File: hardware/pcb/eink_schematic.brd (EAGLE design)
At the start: 90.2 x 71.1 mm, 13 parts, among them J1 AA_BAT_PACKSMD, J2 5.5x2.1mm Barrel, Q1 FDN340P, U1 NUCLEUM, U2 LTC3531ES6-3PBF, U4 MAX6326UR29+

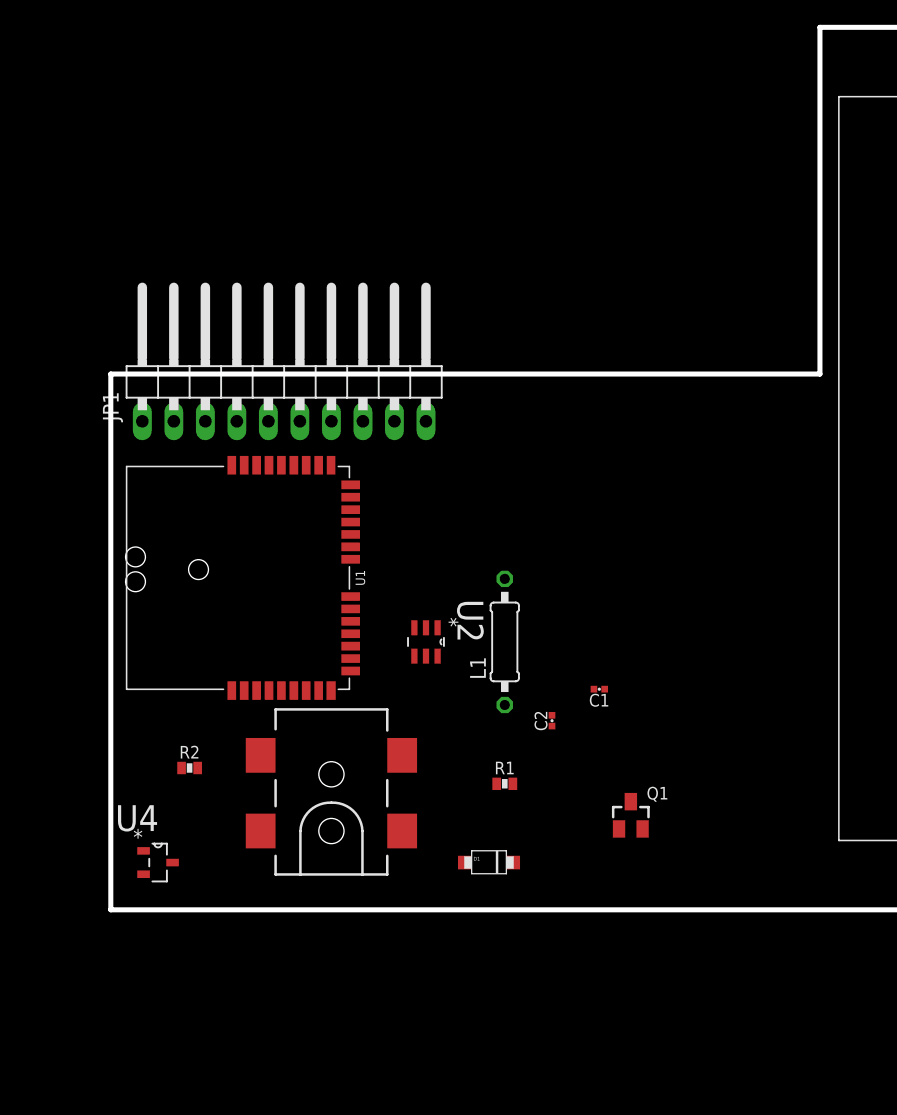
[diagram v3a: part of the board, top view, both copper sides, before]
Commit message: added digikey part numbers for everything
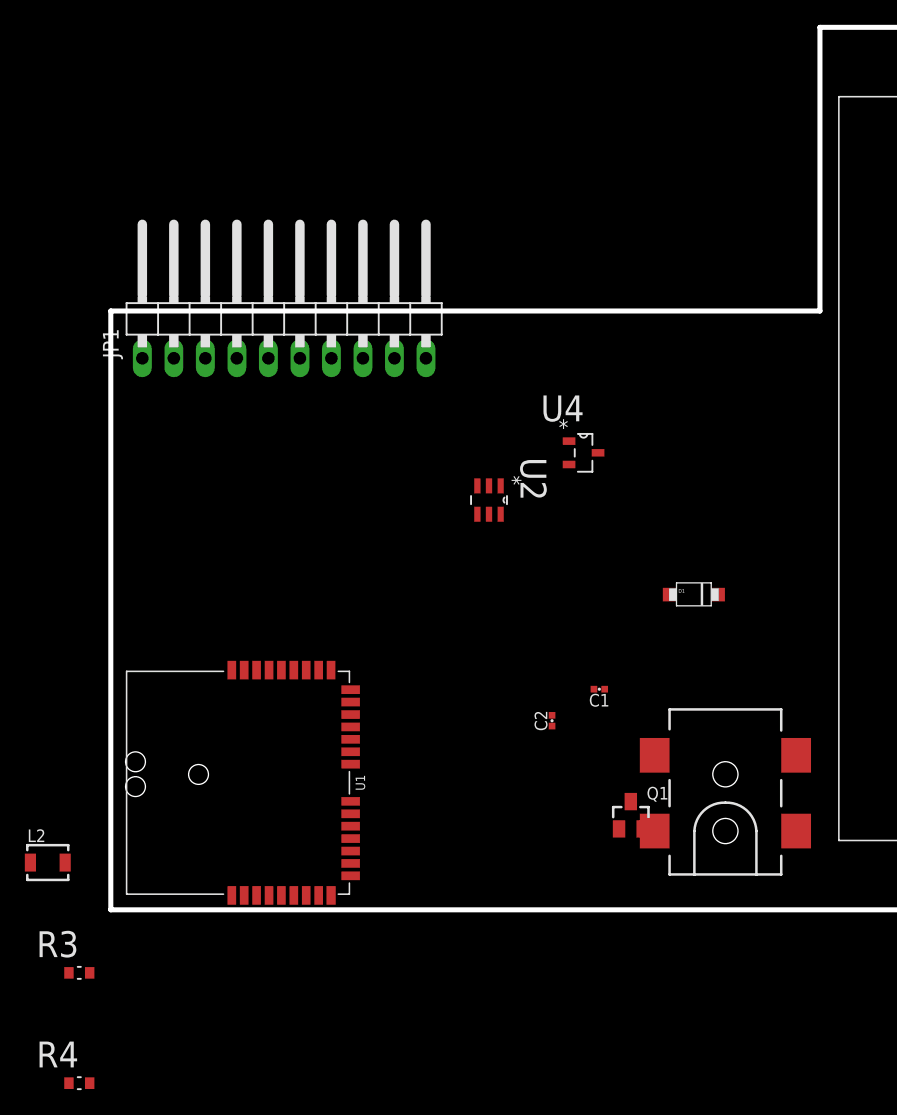
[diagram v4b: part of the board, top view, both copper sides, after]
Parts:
- removed L1: 10uH, umich:0207/10
- removed R1, R2: 100K, passives:0603-RES
- added L2: VLF302510MT, inductor-tdk:VLF302510MT
- added R3, R4: 100K Ohms, Yageo_By_element14_Batch_1:RESC1608X60N
- moved U4 47.6 mm to (38.1, 36.8)
- moved J2 31.8 mm to (49.5, 6.35)
- moved D1 27.2 mm to (47.0, 25.4)
- moved U1 16.5 mm to (1.27, 1.27)
- moved U2 12.5 mm to (30.5, 33.0)
- moved JP1 5.08 mm to (14.0, 48.3)
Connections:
- new net N$6: J2.GND, J2.P$4
- net !SHDN: now also R3.2; no longer R1.1
- net GND: now also R4.2; no longer R2.2
- net N$2: now also R4.1; no longer R2.1
- net N$3: now also R3.1; no longer R1.2
- net SW1: now also L2.2; no longer L1.1
- net SW2: now also L2.1; no longer L1.2
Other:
- outline, holes or cut-outs redrawn

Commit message: Eagle: pretty sure I got things wired up
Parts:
- moved L2 50.8 mm to (38.1, 30.5), turned to 270 degrees
- moved R3 45.8 mm to (30.5, 26.7), turned to 90 degrees
- moved R4 44.0 mm to (29.2, 16.5), turned to 180 degrees
- moved Q1 26.9 mm to (50.8, 33.0)
- moved C1 24.3 mm to (55.9, 35.6), turned to 270 degrees
- moved C2 23.9 mm to (25.4, 36.8)
- moved D1 18.5 mm to (41.9, 43.2)
- moved U1 15.5 mm to (3.81, 16.5)
- moved J2 13.3 mm to (45.7, 19.1)
- moved J1 12.7 mm to (73.7, 48.3)
- moved U4 6.84 mm to (35.6, 43.2)
- moved U2 1.80 mm to (31.8, 34.3)
- moved JP1 1.27 mm to (15.2, 48.3)
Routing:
- net GND: track 0.00 -> 140.2 mm, vias 0 -> 4
- net VCC: track 0.00 -> 74.1 mm
- net N$3: track 0.00 -> 70.1 mm, vias 0 -> 4
- net N$4: track 0.00 -> 43.7 mm, vias 0 -> 2
- net N$2: track 0.00 -> 39.5 mm, vias 0 -> 2
- net !CS: track 0.00 -> 38.5 mm, vias 0 -> 2
- net ENABLE: track 0.00 -> 38.3 mm, vias 0 -> 1
- net TC_BUSY: track 0.00 -> 30.3 mm, vias 0 -> 2
- net SPI_MISO: track 0.00 -> 30.2 mm, vias 0 -> 2
- net SPI_MOSI: track 0.00 -> 27.0 mm, vias 0 -> 2
- net SPI_CLK: track 0.00 -> 21.9 mm
- net N$1: track 0.00 -> 20.7 mm
- net SW1: track 0.00 -> 14.5 mm, vias 0 -> 2
- net N$5: track 0.00 -> 14.2 mm
- net SW2: track 0.00 -> 10.2 mm, vias 0 -> 2
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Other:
- board size 90.2 x 71.1 mm -> 91.4 x 71.1 mm

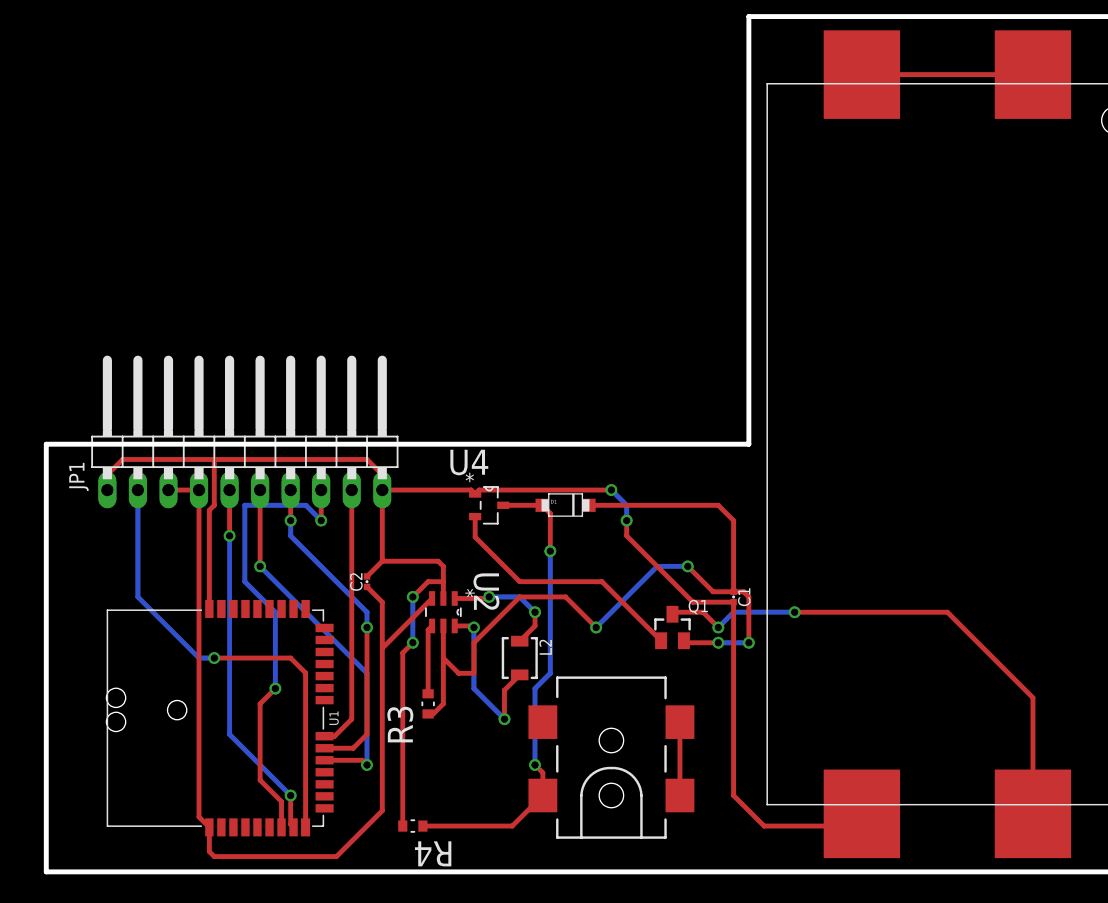
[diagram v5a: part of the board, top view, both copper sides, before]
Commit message: deleted traces from 1st try
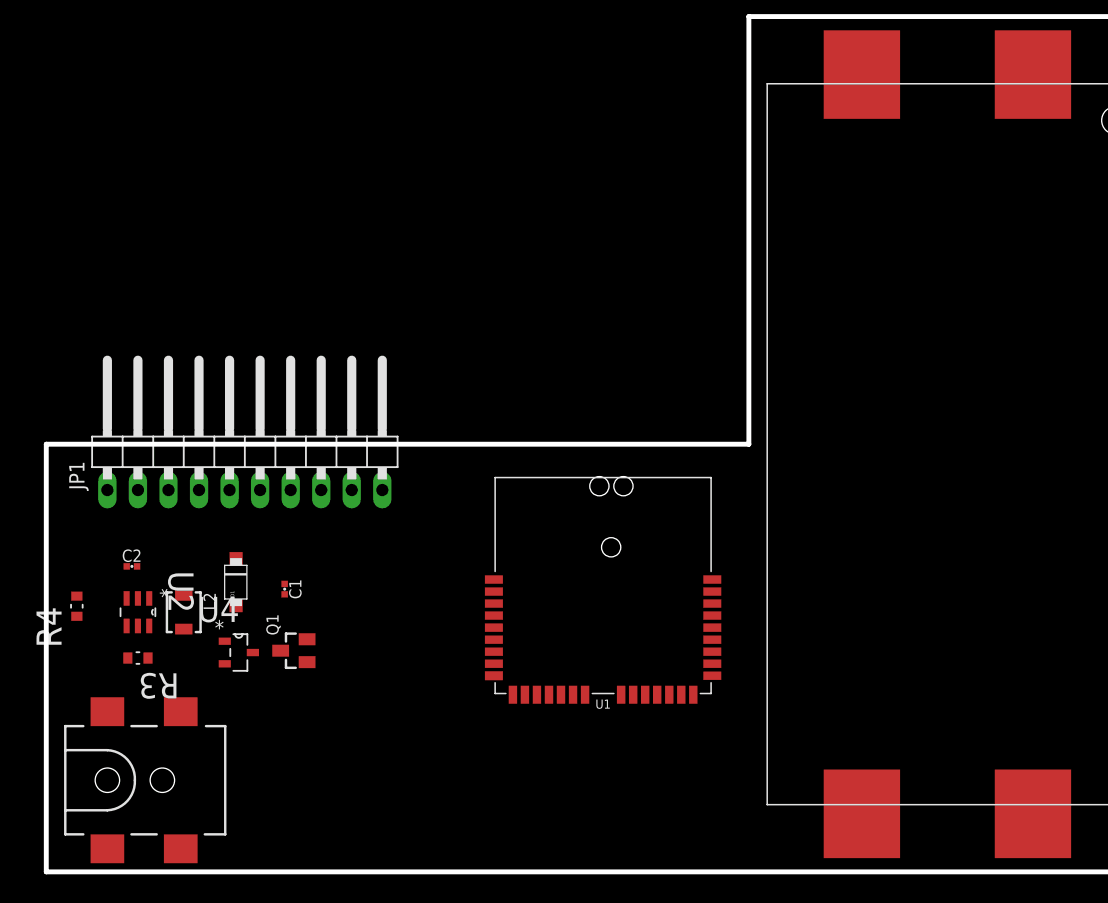
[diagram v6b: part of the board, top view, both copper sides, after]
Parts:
- moved U1 43.4 mm to (36.1, 45.5), turned to 270 degrees
- moved J2 41.9 mm to (3.81, 20.3), turned to 0 degrees
- moved C1 37.3 mm to (18.6, 36.2)
- moved R4 33.4 mm to (1.27, 34.8), turned to 90 degrees
- moved Q1 31.5 mm to (19.3, 31.1), turned to 90 degrees
- moved L2 28.2 mm to (10.2, 34.3)
- moved D1 28.1 mm to (14.5, 36.8), turned to 90 degrees
- moved U2 25.4 mm to (6.35, 34.3)
- moved R3 24.4 mm to (6.35, 30.5), turned to 180 degrees
- moved U4 24.2 mm to (14.7, 30.9)
- moved C2 19.6 mm to (5.85, 38.1), turned to 0 degrees
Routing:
- net GND: track 140.2 -> 0.00 mm, vias 4 -> 0
- net VCC: track 74.1 -> 0.00 mm
- net N$3: track 70.1 -> 0.00 mm, vias 4 -> 0
- net N$4: track 43.7 -> 0.00 mm, vias 2 -> 0
- net N$2: track 39.5 -> 0.00 mm, vias 2 -> 0
- net !CS: track 38.5 -> 0.00 mm, vias 2 -> 0
- net ENABLE: track 38.3 -> 0.00 mm, vias 1 -> 0
- net TC_BUSY: track 30.3 -> 0.00 mm, vias 2 -> 0
- net SPI_MISO: track 30.2 -> 0.00 mm, vias 2 -> 0
- net SPI_MOSI: track 27.0 -> 0.00 mm, vias 2 -> 0
- net SPI_CLK: track 21.9 -> 0.00 mm
- net N$1: track 20.7 -> 0.00 mm
- net SW1: track 14.5 -> 0.00 mm, vias 2 -> 0
- net N$5: track 14.2 -> 0.00 mm
- net SW2: track 10.2 -> 0.00 mm, vias 2 -> 0
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
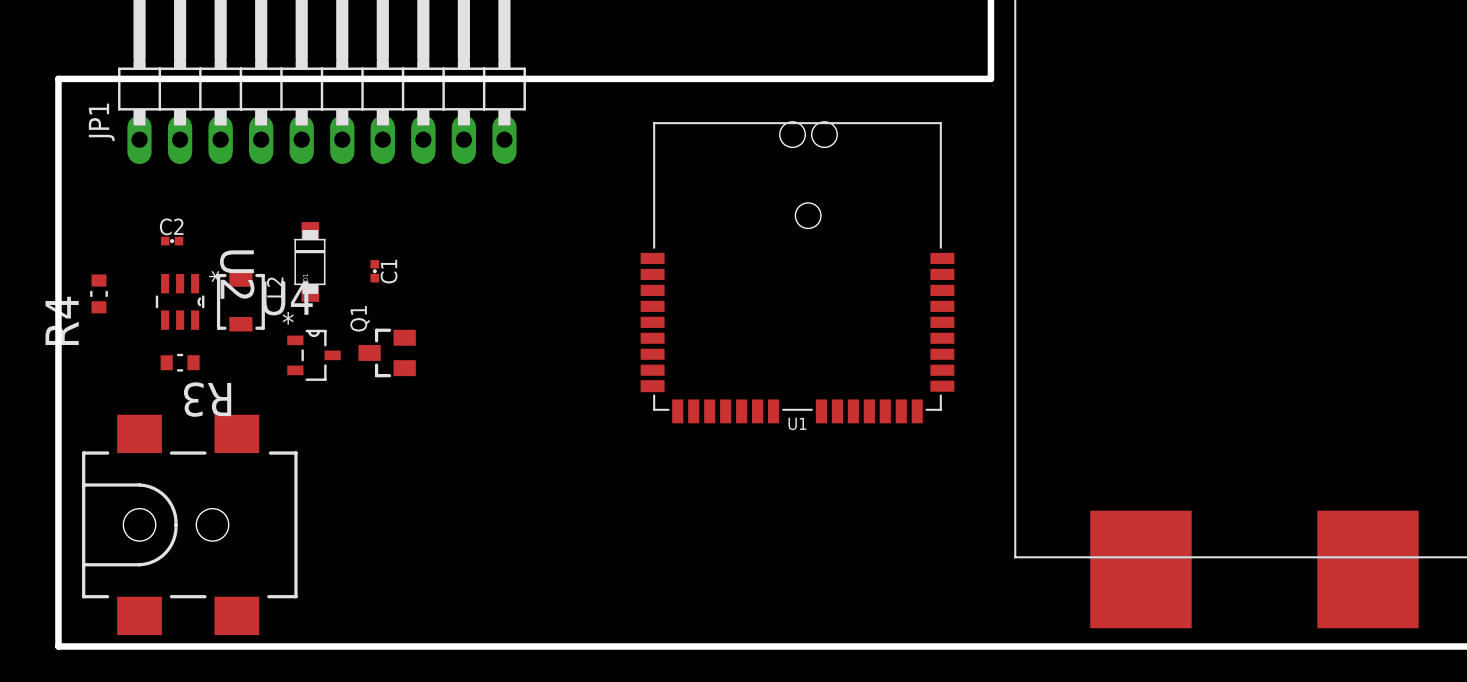
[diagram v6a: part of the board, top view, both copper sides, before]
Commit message: Traces try #2 looks much better
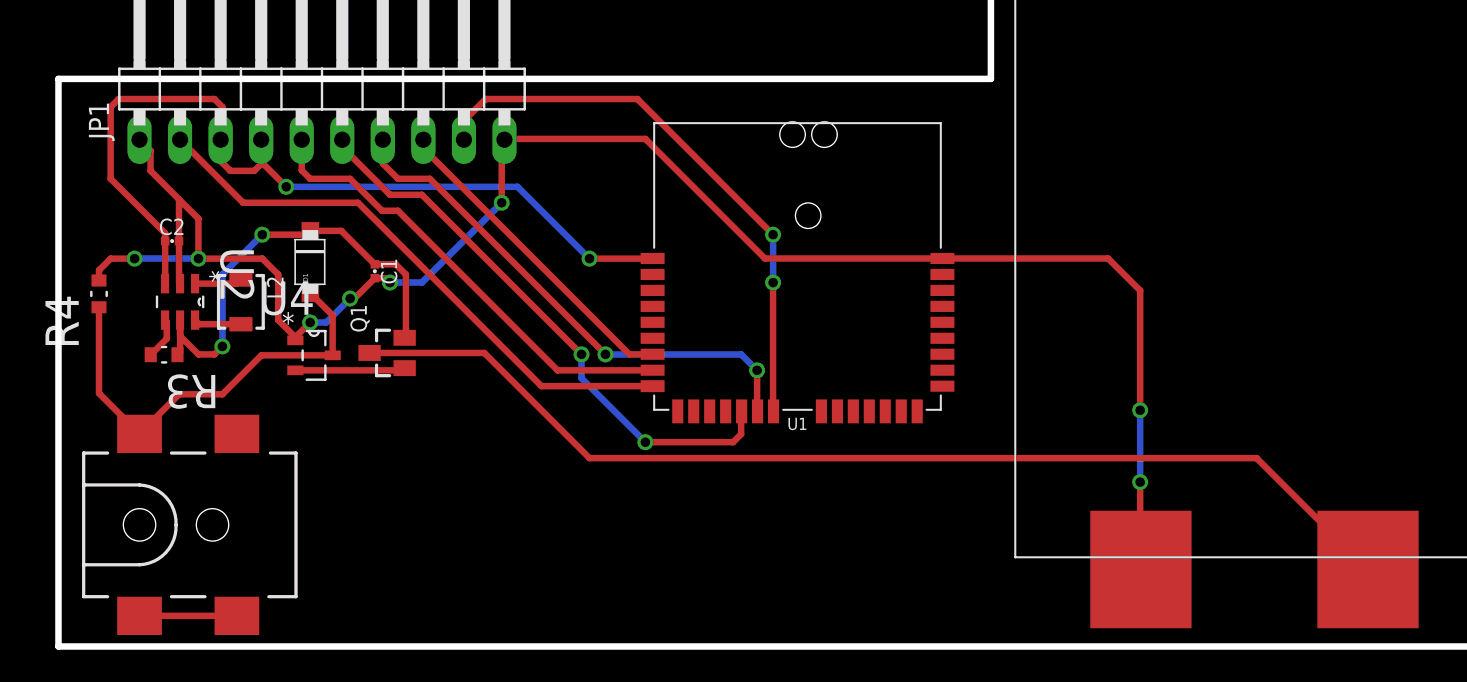
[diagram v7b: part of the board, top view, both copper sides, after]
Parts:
- moved R3 1.12 mm to (5.35, 31.0)
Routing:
- net GND: track 0.00 -> 113.4 mm, vias 0 -> 8
- net N$4: track 0.00 -> 68.2 mm
- net VCC: track 0.00 -> 54.8 mm, vias 0 -> 2
- net ENABLE: track 0.00 -> 36.0 mm
- net SPI_CLK: track 0.00 -> 35.7 mm, vias 0 -> 2
- net SPI_MISO: track 0.00 -> 35.6 mm, vias 0 -> 2
- net SPI_MOSI: track 0.00 -> 32.9 mm, vias 0 -> 2
- net TC_BUSY: track 0.00 -> 29.1 mm
- net N$3: track 0.00 -> 28.8 mm, vias 0 -> 2
- net N$2: track 0.00 -> 27.6 mm
- net !CS: track 0.00 -> 20.3 mm
- net N$1: track 0.00 -> 6.91 mm
- net N$6: track 0.00 -> 6.10 mm
- net SW2: track 0.00 -> 2.98 mm
- net SW1: track 0.00 -> 2.98 mm
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
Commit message: Corrected spacing
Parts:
- moved J2 6.50 mm to (-2.69, 20.3)
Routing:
- net N$2: track 27.6 -> 33.3 mm
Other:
- board size 91.4 x 71.1 mm -> 97.9 x 71.1 mm
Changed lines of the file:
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@@
 <board>
 <plain>
-<wire x1="-1.27" y1="12.7" x2="90.17" y2="12.7" width="0.4064" layer="20"/>
+<wire x1="-7.77" y1="12.7" x2="90.17" y2="12.7" width="0.4064" layer="20"/>
 <wire x1="90.17" y1="12.7" x2="90.17" y2="83.82" width="0.4064" layer="20"/>
 <wire x1="90.17" y1="83.82" x2="57.15" y2="83.82" width="0.4064" layer="20"/>
 <wire x1="57.15" y1="83.82" x2="57.15" y2="48.26" width="0.4064" layer="20"/>
-<wire x1="57.15" y1="48.26" x2="-1.27" y2="48.26" width="0.4064" layer="20"/>
-<wire x1="-1.27" y1="48.26" x2="-1.27" y2="12.7" width="0.4064" layer="20"/>
+<wire x1="57.15" y1="48.26" x2="-7.77" y2="48.26" width="0.4064" layer="20"/>
+<wire x1="-7.77" y1="48.26" x2="-7.77" y2="12.7" width="0.4064" layer="20"/>
+<dimension x1="2.5" y1="55.5" x2="-7.5" y2="55.5" x3="-2.5" y3="54.5" textsize="1.778" layer="20"/>
 </plain>
 <attributes>
@@
 <attribute name="DIGIKEY" value="MAX6326UR29+TCT-ND" x="14.74" y="30.94" size="1.778" layer="27" display="off"/>
 </element>
-<element name="J2" library="SparkFun-Connectors" package="POWER_JACK_SMD" value="5.5x2.1mm Barrel" x="3.81" y="20.32">
-<attribute name="SF_ID" value="PRT-12748" x="3.81" y="20.32" size="1.778" layer="27" display="off"/>
-<attribute name="PROD_ID" value="CONN-08106" x="3.81" y="20.32" size="1.778" layer="27" display="off"/>
-<attribute name="DIGIKEY" value="CP-002AHPJCT-ND" x="3.81" y="20.32" size="1.778" layer="27" display="off"/>
+<element name="J2" library="SparkFun-Connectors" package="POWER_JACK_SMD" value="5.5x2.1mm Barrel" x="-2.69" y="20.32">
+<attribute name="SF_ID" value="PRT-12748" x="-2.69" y="20.32" size="1.778" layer="27" display="off"/>
+<attribute name="PROD_ID" value="CONN-08106" x="-2.69" y="20.32" size="1.778" layer="27" display="off"/>
+<attribute name="DIGIKEY" value="CP-002AHPJCT-ND" x="-2.69" y="20.32" size="1.778" layer="27" display="off"/>
 </element>
 <element name="L2" library="inductor-tdk" package="VLF302510MT" value="VLF302510MT" x="10.16" y="34.29" rot="R270">
@@
 <contactref element="U4" pad="3"/>
 <contactref element="R4" pad="1"/>
-<wire x1="1.27" y1="33.9518" x2="1.27" y2="28.56" width="0.4064" layer="1"/>
-<wire x1="1.27" y1="28.56" x2="3.81" y2="26.02" width="0.4064" layer="1"/>
 <wire x1="15.9084" y1="30.94" x2="15.9084" y2="33.4416" width="0.4064" layer="1"/>
 <wire x1="15.9084" y1="33.4416" x2="14.51" y2="34.84" width="0.4064" layer="1"/>
 <wire x1="15.9084" y1="30.94" x2="11.44" y2="30.94" width="0.4064" layer="1"/>
 <wire x1="11.44" y1="30.94" x2="9" y2="28.5" width="0.4064" layer="1"/>
-<wire x1="9" y1="28.5" x2="6.29" y2="28.5" width="0.4064" layer="1"/>
-<wire x1="6.29" y1="28.5" x2="3.81" y2="26.02" width="0.4064" layer="1"/>
+<wire x1="-2.69" y1="26.02" x2="-2.69" y2="29.9918" width="0.4064" layer="1"/>
+<wire x1="-2.69" y1="29.9918" x2="1.27" y2="33.9518" width="0.4064" layer="1"/>
+<wire x1="1.27" y1="33.9518" x2="1.27" y2="31.73" width="0.4064" layer="1"/>
+<wire x1="1.27" y1="31.73" x2="4.5" y2="28.5" width="0.4064" layer="1"/>
+<wire x1="4.5" y1="28.5" x2="9" y2="28.5" width="0.4064" layer="1"/>
 </signal>
 <signal name="N$3">
@@
 <contactref element="J2" pad="GND"/>
 <contactref element="J2" pad="P$4"/>
-<wire x1="3.81" y1="14.62" x2="9.91" y2="14.62" width="0.4064" layer="1"/>
+<wire x1="-2.69" y1="14.62" x2="3.41" y2="14.62" width="0.4064" layer="1"/>
 </signal>
 <signal name="N$4">
